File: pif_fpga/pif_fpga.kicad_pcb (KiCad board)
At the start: 2 copper layers, 35 x 41 mm, 61 parts, among them P1 CONN_02X20, P2 CONN_01X18, P3 CONN_01X06, P4 CONN_01X05, U1 Si5351A, U2 LCMXO2-2000HC, U3 STM32F070CBT6, U4 W25Q128JVPIQ, U5 74LVC1G14, Y1 25 MHz

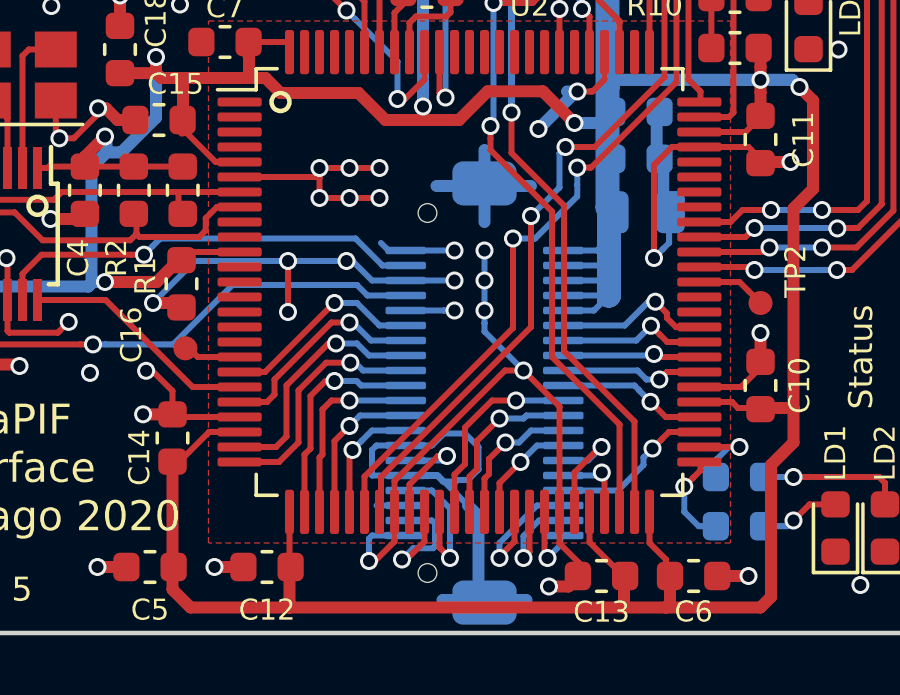
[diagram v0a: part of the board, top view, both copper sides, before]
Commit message: no copper fill under the connector
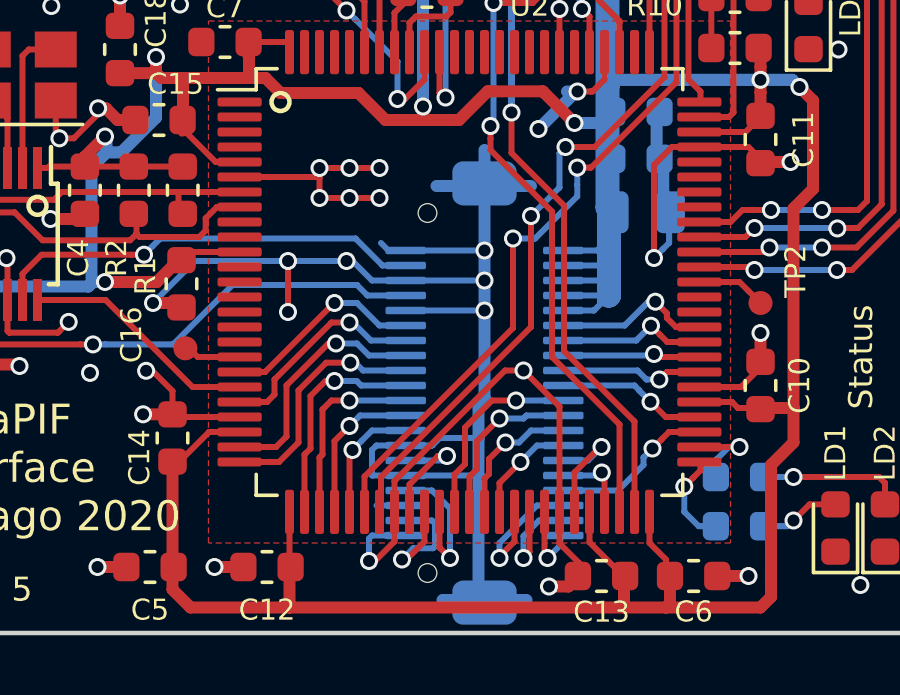
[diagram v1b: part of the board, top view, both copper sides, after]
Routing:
- net GND: track 214.3 -> 218.9 mm, vias 87 -> 84
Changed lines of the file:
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@@
     (thickness 1.6)
     (drawings 45)
-    (tracks 1225)
+    (tracks 1211)
     (zones 0)
     (modules 61)
@@
   (segment (start 150.1 128.9) (end 152.37 128.9) (width 0.2) (layer F.Cu) (net 39))
   (segment (start 152.37 128.9) (end 155.27 131.8) (width 0.2) (layer F.Cu) (net 39))
-  (segment (start 165 125.1) (end 165 126.3) (width 0.4) (layer B.Cu) (net 40))
   (segment (start 165 125.1) (end 166.55 125.1) (width 0.4) (layer B.Cu) (net 40))
   (segment (start 165 125.1) (end 165 123.9) (width 0.4) (layer B.Cu) (net 40))
@@
   (segment (start 161.25 128.25) (end 160.6 127.6) (width 0.2) (layer B.Cu) (net 40))
   (segment (start 162.475 128.25) (end 161.25 128.25) (width 0.2) (layer B.Cu) (net 40))
-  (segment (start 164.450001 135.750001) (end 164.799999 136.099999) (width 0.4) (layer B.Cu) (net 40))
-  (segment (start 164.799999 136.099999) (end 164.799999 138.699999) (width 0.4) (layer B.Cu) (net 40))
-  (segment (start 164.799999 138.699999) (end 165 138.9) (width 0.4) (layer B.Cu) (net 40))
   (segment (start 165 138.9) (end 163.6 138.9) (width 0.4) (layer B.Cu) (net 40))
   (segment (start 165 138.9) (end 166.4 138.9) (width 0.4) (layer B.Cu) (net 40))
@@
   (segment (start 156.8 124.8) (end 159.5 124.8) (width 0.2) (layer F.Cu) (net 40))
   (via (at 159.5 125.5) (size 0.6) (drill 0.4) (layers F.Cu B.Cu) (net 40))
-  (segment (start 165 129.674264) (end 165 129.25) (width 0.2) (layer B.Cu) (net 40))
-  (segment (start 165 129.950006) (end 165 129.674264) (width 0.2) (layer B.Cu) (net 40))
-  (segment (start 166.3 131.250006) (end 165 129.950006) (width 0.2) (layer B.Cu) (net 40))
-  (segment (start 165 128.25) (end 165 129.25) (width 0.2) (layer B.Cu) (net 40))
   (via (at 165 129.25) (size 0.6) (drill 0.4) (layers F.Cu B.Cu) (net 40))
-  (segment (start 165 127.25) (end 165 128.25) (width 0.2) (layer B.Cu) (net 40))
   (via (at 165 128.25) (size 0.6) (drill 0.4) (layers F.Cu B.Cu) (net 40))
   (via (at 165 127.25) (size 0.6) (drill 0.4) (layers F.Cu B.Cu) (net 40))
-  (segment (start 163.999982 127.25) (end 163.999991 127.249991) (width 0.2) (layer B.Cu) (net 40))
-  (segment (start 162.475 127.25) (end 163.999982 127.25) (width 0.2) (layer B.Cu) (net 40))
-  (via (at 163.999991 127.249991) (size 0.6) (drill 0.4) (layers F.Cu B.Cu) (net 40))
-  (segment (start 162.475 128.25) (end 164.000002 128.25) (width 0.2) (layer B.Cu) (net 40))
-  (via (at 164.000002 128.25) (size 0.6) (drill 0.4) (layers F.Cu B.Cu) (net 40))
-  (segment (start 163.65 129.25) (end 164 129.25) (width 0.2) (layer B.Cu) (net 40))
-  (via (at 164 129.25) (size 0.6) (drill 0.4) (layers F.Cu B.Cu) (net 40))
   (segment (start 163.05 112.65) (end 162.05 112.65) (width 0.4) (layer F.Cu) (net 40))
   (via (at 163.05 112.65) (size 0.6) (drill 0.4) (layers F.Cu B.Cu) (net 40))
@@
   (segment (start 167.5 136) (end 167.5 132.450006) (width 0.2) (layer F.Cu) (net 40) (status 10))
   (via (at 166.3 131.250006) (size 0.6) (drill 0.4) (layers F.Cu B.Cu) (net 40))
-  (segment (start 164.450001 135.750001) (end 163.45 134.75) (width 0.2) (layer B.Cu) (net 40))
-  (segment (start 163.45 134.75) (end 162.475 134.75) (width 0.2) (layer B.Cu) (net 40) (status 20))
   (segment (start 147.5 131.05) (end 146.65 130.2) (width 0.4) (layer F.Cu) (net 40))
   (segment (start 149.5 131.05) (end 147.5 131.05) (width 0.4) (layer F.Cu) (net 40))
@@
   (segment (start 162.475 127.25) (end 161.8 127.25) (width 0.2) (layer B.Cu) (net 40) (status 10))
   (segment (start 161.8 127.25) (end 161.55 127) (width 0.2) (layer B.Cu) (net 40))
-  (segment (start 162.475 129.25) (end 163.65 129.25) (width 0.2) (layer B.Cu) (net 40) (status 10))
   (via (at 150 106.2) (size 0.6) (drill 0.4) (layers F.Cu B.Cu) (net 40))
   (segment (start 151 106.2) (end 150 106.2) (width 0.4) (layer B.Cu) (net 40))
@@
   (segment (start 161.25 133.9) (end 161.25 134.75) (width 0.2) (layer B.Cu) (net 40))
   (segment (start 161.4 133.75) (end 161.25 133.9) (width 0.2) (layer B.Cu) (net 40))
-  (segment (start 164.05 134.9) (end 164.45 134.9) (width 0.2) (layer B.Cu) (net 40))
-  (segment (start 164.35 133.35) (end 163.65 133.35) (width 0.2) (layer B.Cu) (net 40))
-  (segment (start 164.05 134.95) (end 164.05 134.9) (width 0.2) (layer B.Cu) (net 40))
-  (segment (start 163.25 133.75) (end 161.4 133.75) (width 0.2) (layer B.Cu) (net 40))
-  (segment (start 163.61199 134.95) (end 164.05 134.95) (width 0.2) (layer B.Cu) (net 40))
-  (segment (start 163.41199 134.75) (end 163.61199 134.95) (width 0.2) (layer B.Cu) (net 40))
-  (segment (start 162.475 134.75) (end 163.41199 134.75) (width 0.2) (layer B.Cu) (net 40))
-  (segment (start 164.8 133.8) (end 164.35 133.35) (width 0.2) (layer B.Cu) (net 40))
-  (segment (start 164.45 134.9) (end 164.8 134.55) (width 0.2) (layer B.Cu) (net 40))
-  (segment (start 164.8 134.55) (end 164.8 133.8) (width 0.2) (layer B.Cu) (net 40))
-  (segment (start 163.65 133.35) (end 163.25 133.75) (width 0.2) (layer B.Cu) (net 40))
   (segment (start 160.315 104.71) (end 162.85 104.71) (width 0.8) (layer F.Cu) (net 40))
   (segment (start 154.18 103) (end 153.925 102.745) (width 0.2) (layer F.Cu) (net 40))
@@
   (segment (start 147.09 99.935) (end 147.39 99.935) (width 0.4) (layer F.Cu) (net 40))
   (segment (start 146.675 100.35) (end 147.09 99.935) (width 0.4) (layer F.Cu) (net 40))
+  (segment (start 161.4 133.75) (end 162.375 133.75) (width 0.2) (layer B.Cu) (net 40))
+  (segment (start 165 125.1) (end 165 129.25) (width 0.4) (layer B.Cu) (net 40))
+  (segment (start 164.799999 138.699999) (end 165 138.9) (width 0.4) (layer B.Cu) (net 40))
+  (segment (start 162.375 127.25) (end 165 127.25) (width 0.2) (layer B.Cu) (net 40))
+  (segment (start 162.375 128.25) (end 165 128.25) (width 0.2) (layer B.Cu) (net 40))
+  (segment (start 162.375 129.25) (end 165 129.25) (width 0.2) (layer B.Cu) (net 40))
+  (segment (start 163.26 133.75) (end 162.375 133.75) (width 0.2) (layer B.Cu) (net 40))
+  (segment (start 164.799999 133.500001) (end 163.509999 133.500001) (width 0.2) (layer B.Cu) (net 40))
+  (segment (start 163.509999 133.500001) (end 163.26 133.75) (width 0.2) (layer B.Cu) (net 40))
+  (segment (start 164.799999 134.729999) (end 164.799999 138.699999) (width 0.4) (layer B.Cu) (net 40))
+  (segment (start 164.779998 134.75) (end 162.375 134.75) (width 0.2) (layer B.Cu) (net 40))
+  (segment (start 164.799999 134.729999) (end 164.779998 134.75) (width 0.2) (layer B.Cu) (net 40))
+  (segment (start 164.799999 133.500001) (end 164.799999 134.729999) (width 0.4) (layer B.Cu) (net 40))
+  (segment (start 164.799999 132.350001) (end 164.799999 133.500001) (width 0.4) (layer B.Cu) (net 40))
+  (segment (start 165 129.25) (end 165 132.15) (width 0.4) (layer B.Cu) (net 40))
+  (segment (start 165 132.15) (end 164.799999 132.350001) (width 0.4) (layer B.Cu) (net 40))
   (segment (start 155.6 101.45) (end 156.5 101.45) (width 0.4) (layer F.Cu) (net 41))
   (segment (start 147.1 110.4) (end 148.225 111.525) (width 0.4) (layer F.Cu) (net 41))
@@
       )
     )
+  )
+  (zone (net 0) (net_name "") (layer B.Cu) (hatch edge 0.508)
+    (connect_pads (clearance 0.25))
+    (min_thickness 0.254)
+    (keepout (tracks allowed) (vias allowed) (copperpour not_allowed))
+    (fill (arc_segments 32) (thermal_gap 0.508) (thermal_bridge_width 0.508))
+    (polygon
+      (pts
+        (xy 166.76 137.9) (xy 163.245 137.9) (xy 163.2375 126.24) (xy 166.7625 126.24)
+      )
+    )

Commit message: - updated revision infos - changed some traces
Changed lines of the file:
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@@
     (thickness 1.6)
     (drawings 45)
-    (tracks 1211)
+    (tracks 1215)
     (zones 0)
     (modules 61)
@@
   (title_block
     (title "UltraPIF FPGA")
-    (date 2018-04-09)
-    (rev 3)
+    (date 2020-03-04)
+    (rev 5)
     (company jago85)
   )
@@
   )
   (setup
-    (last_trace_width 0.2)
+    (last_trace_width 0.4)
     (user_trace_width 0.16)
     (user_trace_width 0.4)
@@
   (segment (start 170.5 137) (end 170.5 136) (width 0.2) (layer F.Cu) (net 41) (status 20))
   (segment (start 169.65 139.150002) (end 171.05 139.150002) (width 0.4) (layer F.Cu) (net 41))
-  (segment (start 158.5 139.150002) (end 169.65 139.150002) (width 0.4) (layer F.Cu) (net 41))
   (segment (start 169.65 138.1) (end 169.65 139.150002) (width 0.4) (layer F.Cu) (net 41) (status 10))
   (segment (start 154.95 121.5) (end 157.15 121.5) (width 0.4) (layer F.Cu) (net 41))
@@
   (segment (start 154.05 120.799996) (end 154.05 122.82) (width 0.4) (layer B.Cu) (net 41))
   (segment (start 154.05 122.82) (end 152.89 123.98) (width 0.4) (layer B.Cu) (net 41))
+  (segment (start 169.349998 139.45) (end 169.649998 139.15) (width 0.4) (layer F.Cu) (net 41))
+  (segment (start 158.81 139.45) (end 169.349998 139.45) (width 0.4) (layer F.Cu) (net 41))
+  (segment (start 169.649998 139.15) (end 169.65 139.150002) (width 0.4) (layer F.Cu) (net 41))
+  (segment (start 158.5 139.150002) (end 158.510002 139.150002) (width 0.4) (layer F.Cu) (net 41))
+  (segment (start 158.510002 139.150002) (end 158.81 139.45) (width 0.4) (layer F.Cu) (net 41))
   (segment (start 157.59999 104.101466) (end 157.425727 104.275729) (width 0.2) (layer B.Cu) (net 42))
   (segment (start 170.5 102.75) (end 158.184301 102.75) (width 0.2) (layer B.Cu) (net 42))

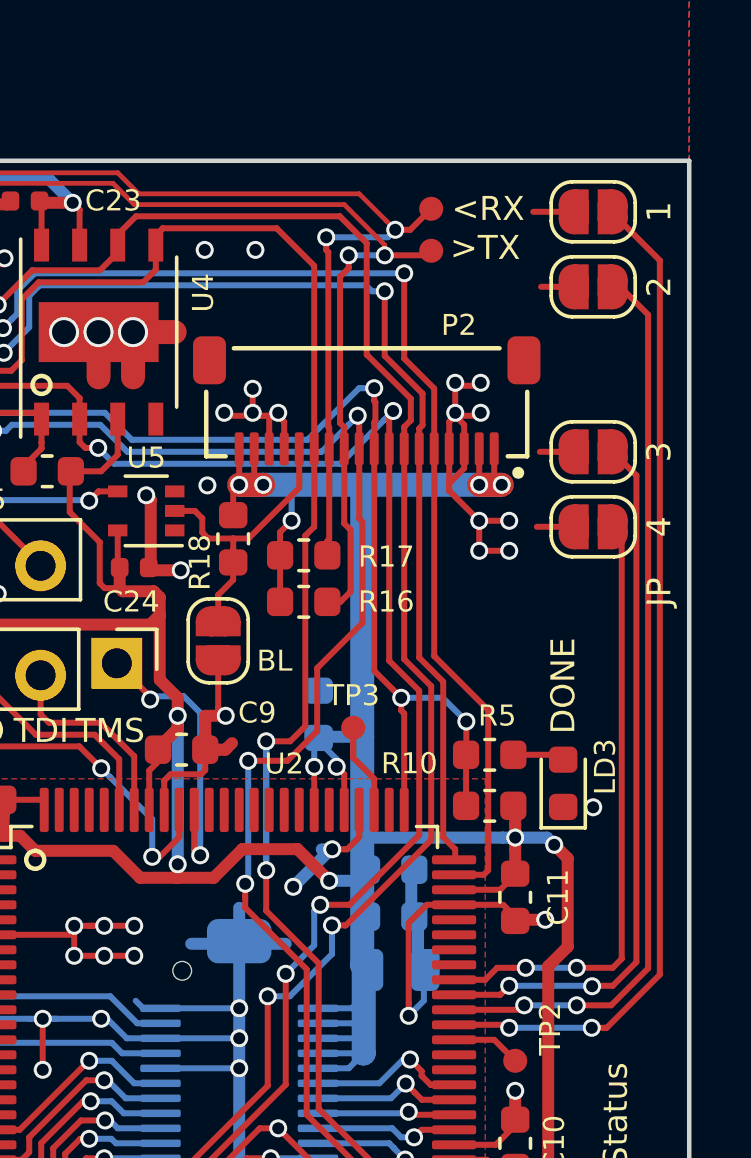
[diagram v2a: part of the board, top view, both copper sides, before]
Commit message: - moved jumpers a bit downwards - no cupper fill under P2
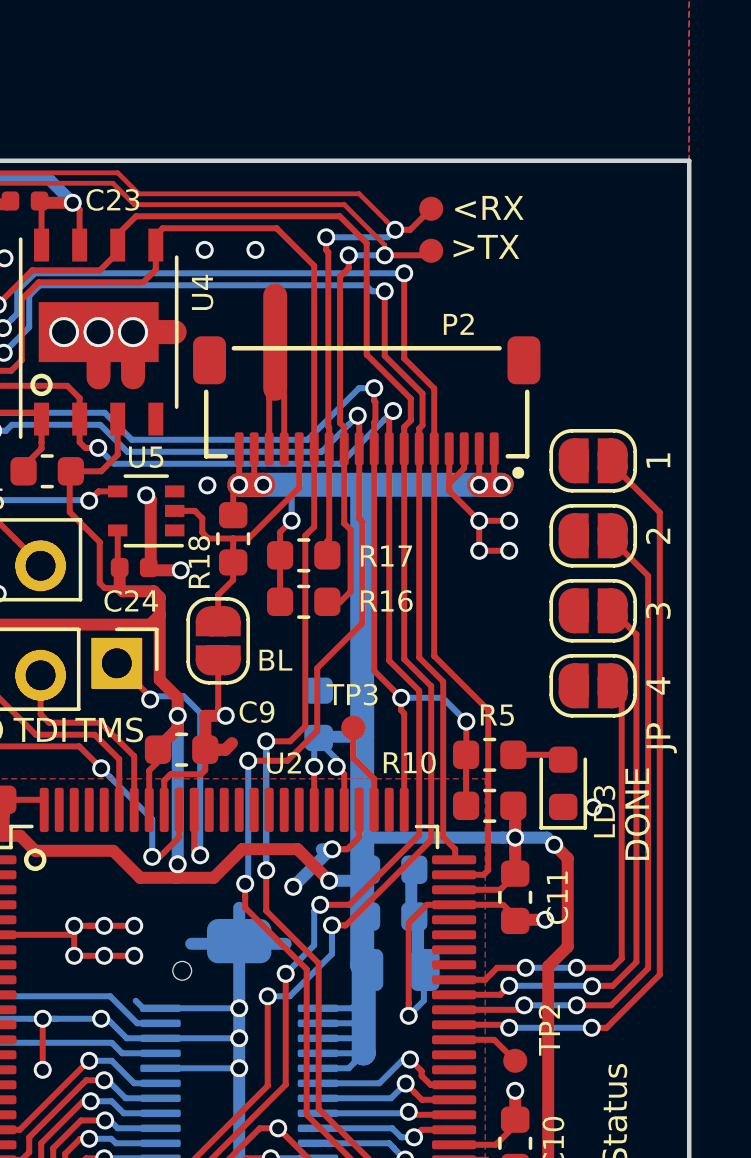
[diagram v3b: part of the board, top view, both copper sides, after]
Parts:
- moved JP1 8.30 mm to (176.8, 109.0)
- moved JP2 8.30 mm to (176.8, 111.5)
- moved JP3 5.30 mm to (176.8, 114.0)
- moved JP4 5.30 mm to (176.8, 116.5)
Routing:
- net GND: track 218.9 -> 210.2 mm, vias 84 -> 76
- net /FPGA/JP2: track 30.7 -> 22.0 mm
- net /FPGA/JP1: track 33.8 -> 25.4 mm
- net /FPGA/JP4: track 20.4 -> 15.1 mm
- net /FPGA/JP3: track 23.8 -> 18.5 mm

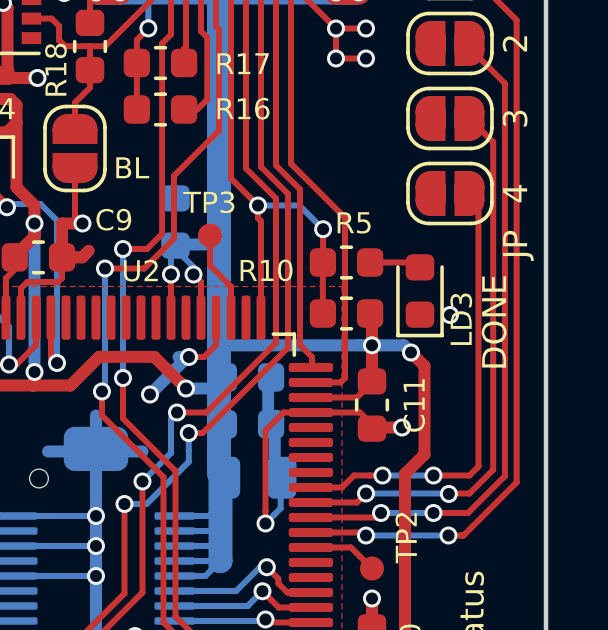
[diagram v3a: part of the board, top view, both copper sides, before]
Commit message: removed via under LD3 silk
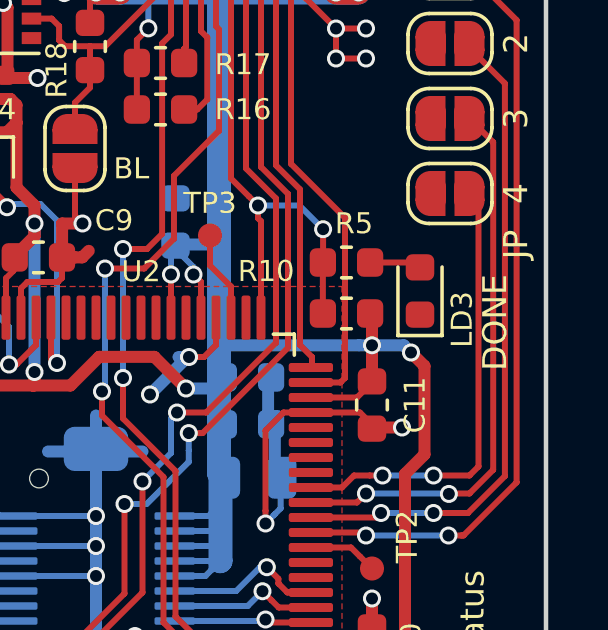
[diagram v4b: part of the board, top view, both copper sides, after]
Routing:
- net GND: vias 76 -> 75
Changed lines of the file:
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@@
     (thickness 1.6)
     (drawings 45)
-    (tracks 1189)
+    (tracks 1188)
     (zones 0)
     (modules 61)
@@
   )
   (setup
-    (last_trace_width 0.8)
+    (last_trace_width 0.2)
     (user_trace_width 0.16)
     (user_trace_width 0.4)
@@
   (via (at 173.8 138.1) (size 0.6) (drill 0.4) (layers F.Cu B.Cu) (net 40))
   (segment (start 172.55 138.1) (end 173.8 138.1) (width 0.4) (layer F.Cu) (net 40))
-  (via (at 176.8 120.55) (size 0.6) (drill 0.4) (layers F.Cu B.Cu) (net 40))
   (via (at 156.65 109.42) (size 0.6) (drill 0.4) (layers F.Cu B.Cu) (net 40))
   (segment (start 163.8675 119.3125) (end 163.8675 118.63) (width 0.2) (layer F.Cu) (net 40))

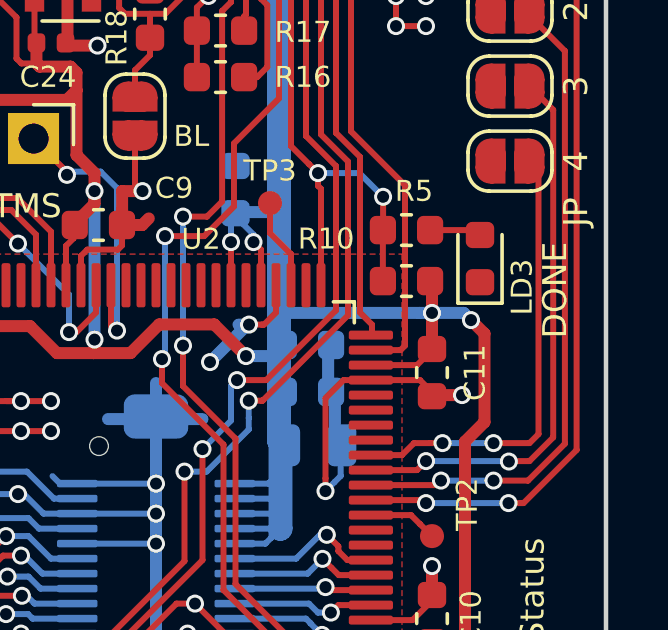
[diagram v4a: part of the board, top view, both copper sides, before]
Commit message: removed unnecessary via from power rail
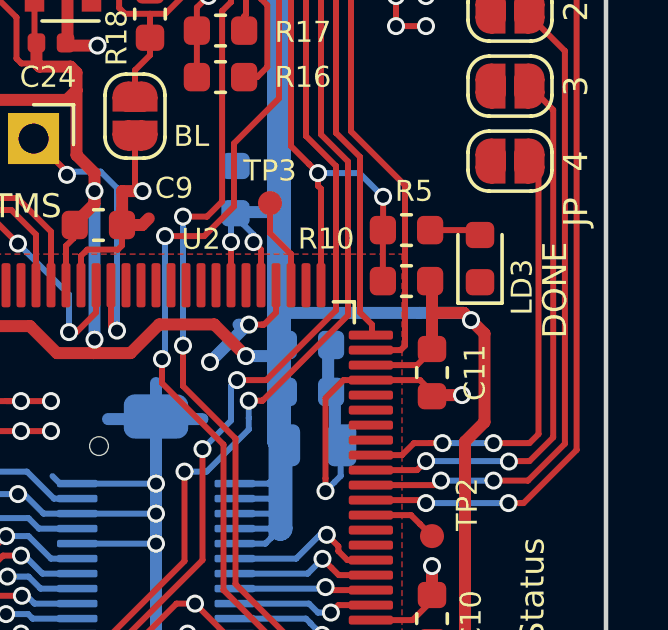
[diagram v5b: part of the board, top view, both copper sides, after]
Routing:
- net +3V3: track 276.6 -> 278.0 mm, vias 19 -> 18
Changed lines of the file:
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@@
     (thickness 1.6)
     (drawings 45)
-    (tracks 1188)
+    (tracks 1189)
     (zones 0)
     (modules 61)
@@
   )
   (setup
-    (last_trace_width 0.2)
+    (last_trace_width 0.4)
     (user_trace_width 0.16)
     (user_trace_width 0.4)
@@
   (segment (start 154.0575 121.3375) (end 154.22 121.5) (width 0.4) (layer F.Cu) (net 41))
   (segment (start 154.22 121.5) (end 154.95 121.5) (width 0.4) (layer F.Cu) (net 41))
-  (via (at 174.200004 121.56) (size 0.6) (drill 0.4) (layers F.Cu B.Cu) (net 41))
   (segment (start 173.77574 121.56) (end 174.200004 121.56) (width 0.4) (layer B.Cu) (net 41))
   (segment (start 174.200004 121.984264) (end 174.200004 121.56) (width 0.4) (layer F.Cu) (net 41))
@@
   (segment (start 158.5 139.150002) (end 158.510002 139.150002) (width 0.4) (layer F.Cu) (net 41))
   (segment (start 158.510002 139.150002) (end 158.81 139.45) (width 0.4) (layer F.Cu) (net 41))
+  (segment (start 175.26 121.56) (end 174.200004 121.56) (width 0.4) (layer F.Cu) (net 41))
+  (segment (start 175.5 121.8) (end 175.26 121.56) (width 0.4) (layer F.Cu) (net 41))
   (segment (start 157.59999 104.101466) (end 157.425727 104.275729) (width 0.2) (layer B.Cu) (net 42))
   (segment (start 170.5 102.75) (end 158.184301 102.75) (width 0.2) (layer B.Cu) (net 42))
